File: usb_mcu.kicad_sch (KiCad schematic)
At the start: 4 parts, among them P1 USB_C_Plug_USB2.0

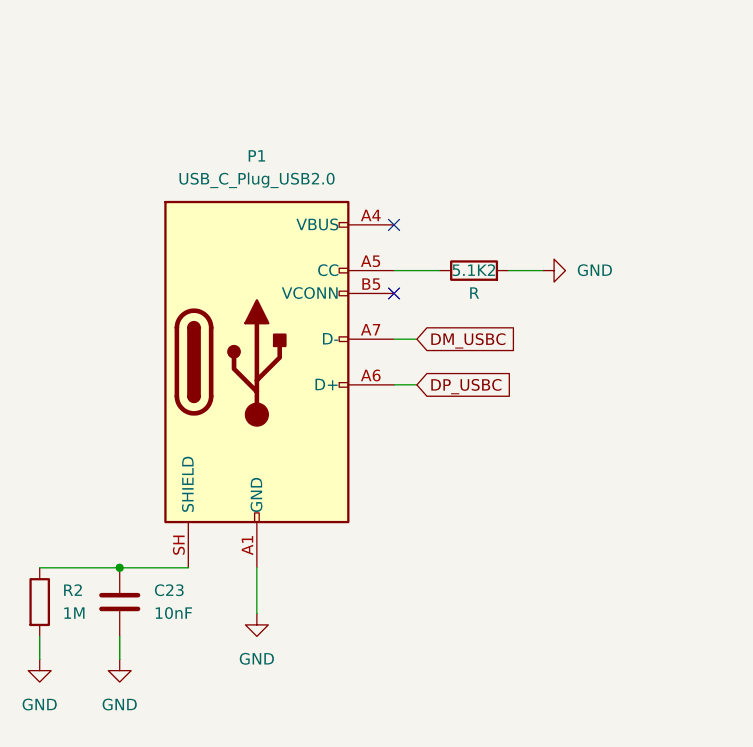
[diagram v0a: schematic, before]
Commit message: added usb mcu and footprints
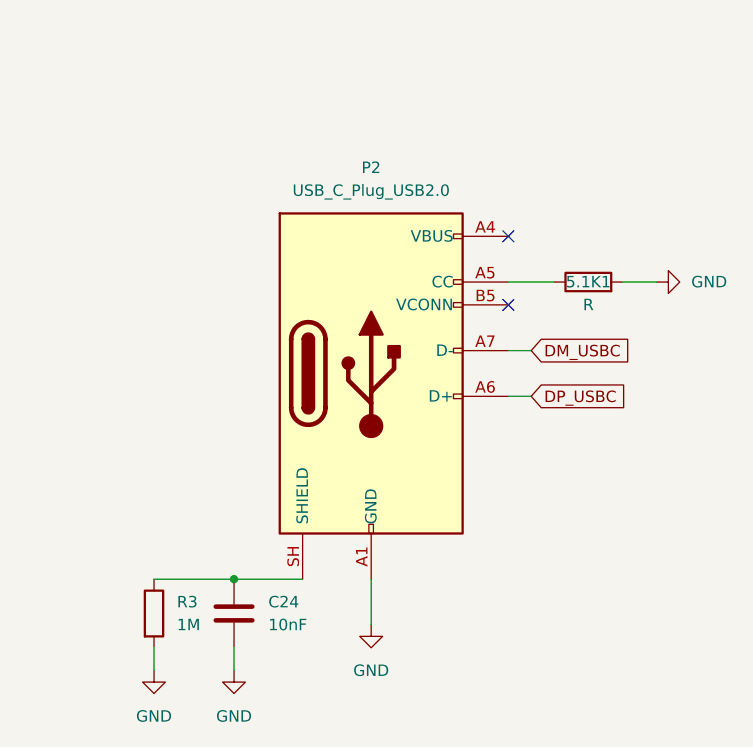
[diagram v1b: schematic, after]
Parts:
- removed 5.1K2: R, symbol Device:R
- removed C23: 10nF, symbol Device:C
- removed P1: USB_C_Plug_USB2.0, Connector_USB:USB_C_Receptacle_HRO_TYPE-C-31-M-12, symbol Connector:USB_C_Plug_USB2.0
- removed R2: 1M, symbol Device:R
- added 5.1K1: R, symbol Device:R
- added C24: 10nF, symbol Device:C
- added P2: USB_C_Plug_USB2.0, Connector_USB:USB_C_Receptacle_HRO_TYPE-C-31-M-12, symbol Connector:USB_C_Plug_USB2.0
- added R3: 1M, symbol Device:R
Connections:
- net DM_USBC: now also P2.A7 (D-)
- net DP_USBC: now also P2.A6 (D+)
- net GND: now also 5.1K1.2, C24.2, P2.A1 (GND), P2.A12 (GND), P2.B1 (GND), P2.B12 (GND), R3.2
- new net: C24.1, P2.SH (SHIELD), R3.1
- new net: P2.A4 (VBUS), P2.A9 (VBUS), P2.B4 (VBUS), P2.B9 (VBUS)
- new net: 5.1K1.1, P2.A5 (CC)

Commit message: added user ports
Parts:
- 5.1K1, R3: footprint (none) -> Resistor_SMD:R_0805_2012Metric_Pad1.20x1.40mm_HandSolder
- C24: footprint (none) -> Capacitor_SMD:C_0805_2012Metric_Pad1.18x1.45mm_HandSolder
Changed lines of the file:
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@@
 			)
 		)
-		(property "Footprint" ""
+		(property "Footprint" "Capacitor_SMD:C_0805_2012Metric_Pad1.18x1.45mm_HandSolder"
 			(at 126.6952 118.11 0)
 			(hide yes)
@@
 			)
 		)
-		(property "Footprint" ""
+		(property "Footprint" "Resistor_SMD:R_0805_2012Metric_Pad1.20x1.40mm_HandSolder"
 			(at 115.062 114.3 90)
 			(hide yes)
@@
 			)
 		)
-		(property "Footprint" ""
+		(property "Footprint" "Resistor_SMD:R_0805_2012Metric_Pad1.20x1.40mm_HandSolder"
 			(at 165.1 79.248 90)
 			(hide yes)

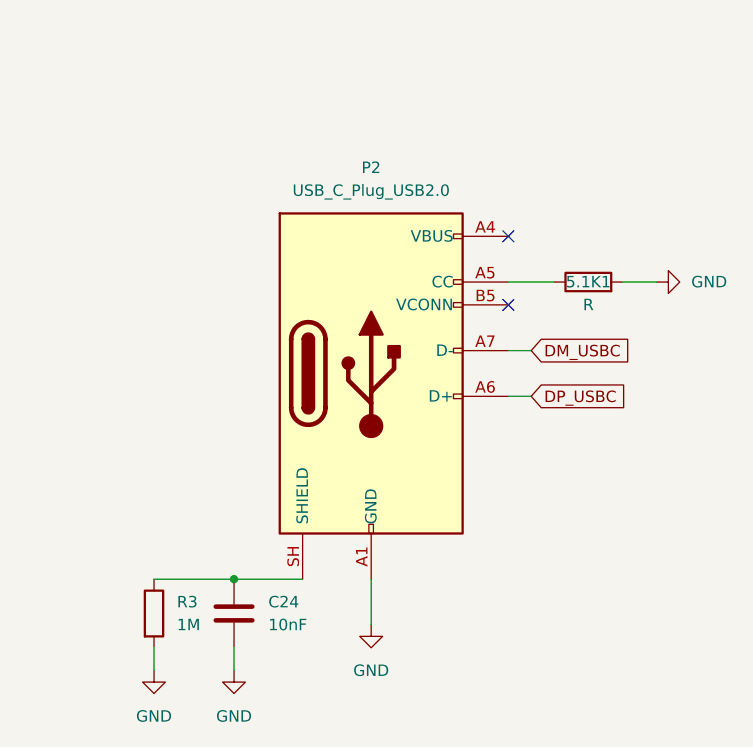
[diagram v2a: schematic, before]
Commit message: added 5v buck converter and place JST PH connectors
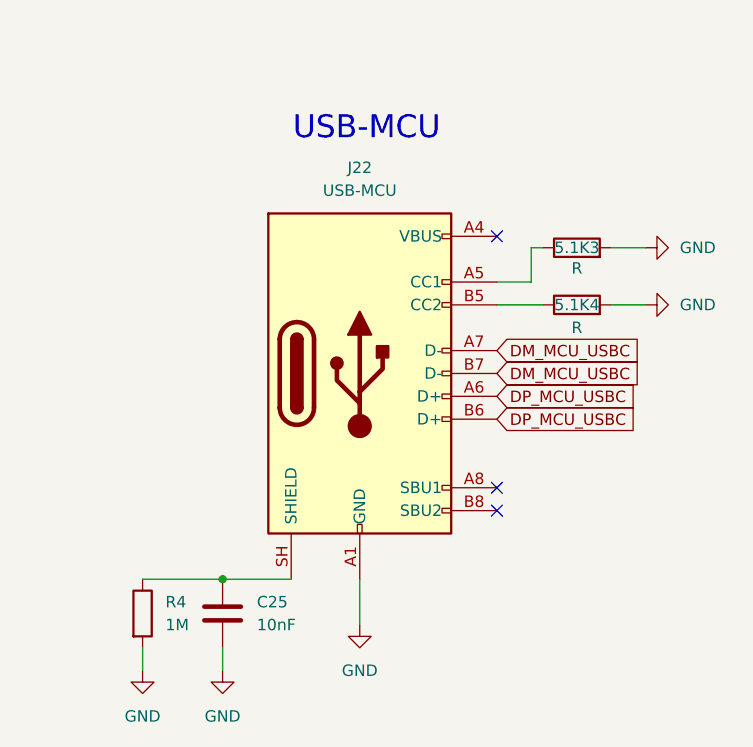
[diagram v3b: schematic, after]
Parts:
- removed 5.1K1: R, Resistor_SMD:R_0805_2012Metric_Pad1.20x1.40mm_HandSolder, symbol Device:R
- removed C24: 10nF, Capacitor_SMD:C_0805_2012Metric_Pad1.18x1.45mm_HandSolder, symbol Device:C
- removed P2: USB_C_Plug_USB2.0, Connector_USB:USB_C_Receptacle_HRO_TYPE-C-31-M-12, symbol Connector:USB_C_Plug_USB2.0
- removed R3: 1M, Resistor_SMD:R_0805_2012Metric_Pad1.20x1.40mm_HandSolder, symbol Device:R
- added 5.1K3, 5.1K4: R, Resistor_SMD:R_0805_2012Metric_Pad1.20x1.40mm_HandSolder, symbol Device:R
- added C25: 10nF, Capacitor_SMD:C_0805_2012Metric_Pad1.18x1.45mm_HandSolder, symbol Device:C
- added J22: USB-MCU, Connector_USB:USB_C_Receptacle_HRO_TYPE-C-31-M-12, symbol Connector:USB_C_Receptacle_USB2.0_16P
- added R4: 1M, Resistor_SMD:R_0805_2012Metric_Pad1.20x1.40mm_HandSolder, symbol Device:R
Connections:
- net GND: now also 5.1K3.2, 5.1K4.2, C25.2, J22.A1 (GND), J22.A12 (GND), J22.B1 (GND), J22.B12 (GND), R4.2
- new net: 5.1K4.1, J22.B5 (CC2)
- new net: J22.A4 (VBUS), J22.A9 (VBUS), J22.B4 (VBUS), J22.B9 (VBUS)
- new net: 5.1K3.1, J22.A5 (CC1)
- new net: C25.1, J22.SH (SHIELD), R4.1
- new net DM_MCU_USBC: J22.A7 (D-), J22.B7 (D-)
- new net DP_MCU_USBC: J22.A6 (D+), J22.B6 (D+)
- no-connect marks 2 -> 3
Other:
- note added: "USB-MCU"

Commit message: change vbat_prot footprint and added pwrmux for 3v3 ubs_mcu connector
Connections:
- net USB_MCU_VBUS: now reaches J22.A4 (VBUS), J22.A9 (VBUS), J22.B4 (VBUS), J22.B9 (VBUS)
- no-connect marks 3 -> 2
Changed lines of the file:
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@@
-	)
-	(no_connect
-		(at 154.94 72.39)
 	)
 	(no_connect
@@
 		(pts
 			(xy 115.57 118.11) (xy 115.57 120.65)
+		)
+		(stroke
+			(width 0)
+			(type default)
+		)
+	)
+	(wire
+		(pts
+			(xy 154.94 67.31) (xy 154.94 72.39)
 		)
 		(stroke
@@
 			(hide yes)
 			(show_name no)
+			(do_not_autoplace no)
+			(effects
+				(font
+					(size 1.27 1.27)
+				)
+				(justify left)
+			)
+		)
+	)
+	(global_label "USB_MCU_VBUS"
+		(shape input)
+		(at 154.94 67.31 90)
+		(fields_autoplaced yes)
+		(effects
+			(font
+				(size 1.27 1.27)
+			)
+			(justify left)
+		)
+		(property "Intersheetrefs" "${INTERSHEET_REFS}"
+			(at 154.94 49.6291 90)
+			(hide yes)
+			(show_name no)
